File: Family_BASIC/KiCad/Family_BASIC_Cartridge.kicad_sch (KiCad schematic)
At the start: 0 parts

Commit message: Schematic started
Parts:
- added IC1: CHR ROM (27C64), Package_DIP:DIP-28_W15.24mm, symbol Memory_EPROM:27C64
- added IC2: PRG ROM (27256), Package_DIP:DIP-28_W15.24mm, symbol Memory_EPROM:27C256
- added IC4: 74HCT20, symbol 74xx:74LS20
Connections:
- new net A0: IC1.10 (A0), IC2.10 (A0)
- new net A1: IC1.9 (A1), IC2.9 (A1)
- new net A10: IC1.21 (A10), IC2.21 (A10)
- new net A11: IC1.23 (A11), IC2.23 (A11)
- new net A12: IC1.2 (A12), IC2.2 (A12)
- new net A13: IC2.26 (A13)
- new net A14: IC2.27 (A14)
- new net A2: IC1.8 (A2), IC2.8 (A2)
- new net A3: IC1.7 (A3), IC2.7 (A3)
- new net A4: IC1.6 (A4), IC2.6 (A4)
- new net A5: IC1.5 (A5), IC2.5 (A5)
- new net A6: IC1.4 (A6), IC2.4 (A6)
- new net A7: IC1.3 (A7), IC2.3 (A7)
- new net A8: IC1.25 (A8), IC2.25 (A8)
- new net A9: IC1.24 (A9), IC2.24 (A9)
- new net GND: IC1.14 (GND), IC2.14 (GND), IC2.20 (~{CE})
- new net PA13: IC1.22 (~{OE})
- new net V_{CC}: IC1.1 (VPP), IC1.27 (~{PGM}), IC1.28 (VCC), IC2.1 (VPP), IC2.28 (VCC)
- new net ~{RD}: IC1.20 (~{CE})
- new net ~{ROMSEL}: IC2.22 (~{OE})

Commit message: Schematic design progression
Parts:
- added BT1: 3V, symbol Device:Battery_Cell
- added C1: 68pF, symbol Device:C
- added C2, C3, C4, C5: 100nF, symbol Device:C
- added D1, D2: D, symbol Device:D
- added H1: Famicom_Cartridge_Edge, famicom:Famicom Cartridge Edge Connector (long legs), symbol Clueless_Engineer:Famicom_Cartridge_Edge
- added IC1: Working RAM (62256), Package_DIP:DIP-28_W15.24mm, symbol Memory_RAM:HM62256BLP
- added R1: 5.1KΩ, symbol Device:R
- renumbered IC4 to IC3, IC1 to IC4
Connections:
- net A13 is gone; now on net A_{13}: IC2.26 (A13)
- net A14 is gone; now on net A_{14}: IC2.27 (A14)
- net GND: now also IC3.10, IC3.12, IC3.13, IC3.7 (GND), IC3.9, BT1.2 (-), C1.2, C2.2, C3.2, C4.2, C5.2, H1.1 (GND), H1.16 (GND), IC1.14 (GND), IC1.22 (~{OE})
- net V_{CC}: now also IC3.14 (VCC), C2.1, C3.1, C4.1, C5.1, H1.30 (VCC), H1.31 (VCC)
- net ~{RD}: now also H1.17 (p~{RD})
- net ~{ROMSEL}: now also IC3.1, H1.44 (~{ROMSEL})
- net A_{13}: now reaches IC3.2
- net A_{13}: now also H1.34 (cA13)
- net A_{14}: now reaches IC3.4
- net A_{14}: now also H1.35 (cA14)
- net at IC3.6: now also C1.1, R1.2
- net PD_{0}: now reaches IC4.11 (D0)
- net PD_{0}: now also H1.26 (pD0)
- net PD_{1}: now reaches IC4.12 (D1)
- net PD_{1}: now also H1.27 (pD1)
- net PD_{2}: now reaches IC4.13 (D2)
- net PD_{2}: now also H1.28 (pD2)
- net PD_{3}: now reaches IC4.15 (D3)
- net PD_{3}: now also H1.29 (pD3)
- net PD_{4}: now reaches IC4.16 (D4)
- net PD_{4}: now also H1.60 (pD4)
- net PD_{5}: now reaches IC4.17 (D5)
- net PD_{5}: now also H1.59 (pD5)
- net PD_{6}: now reaches IC4.18 (D6)
- net PD_{6}: now also H1.58 (pD6)
- net PD_{7}: now reaches IC4.19 (D7)
- net PD_{7}: now also H1.57 (pD7)
- net D_{0}: now reaches IC2.11 (D0)
- net D_{0}: now also H1.43 (cD0), IC1.11 (Q0)
- net D_{1}: now reaches IC2.12 (D1)
- net D_{1}: now also H1.42 (cD1), IC1.12 (Q1)
- net D_{2}: now reaches IC2.13 (D2)
- net D_{2}: now also H1.41 (cD2), IC1.13 (Q2)
- net D_{3}: now reaches IC2.15 (D3)
- net D_{3}: now also H1.40 (cD3), IC1.15 (Q3)
- net D_{4}: now reaches IC2.16 (D4)
- net D_{4}: now also H1.39 (cD4), IC1.16 (Q4)
- net D_{5}: now reaches IC2.17 (D5)
- net D_{5}: now also H1.38 (cD5), IC1.17 (Q5)
- net D_{6}: now reaches IC2.18 (D6)
- net D_{6}: now also H1.37 (cD6), IC1.18 (Q6)
- net D_{7}: now reaches IC2.19 (D7)
- net D_{7}: now also H1.36 (cD7), IC1.19 (Q7)
- net A0 renamed A_{0}
- net A_{0}: now also H1.13 (cA0), IC1.10 (A0); no longer IC4.10 (A0)
- net A1 renamed A_{1}
- net A_{1}: now also H1.12 (cA1), IC1.9 (A1); no longer IC4.9 (A1)
- net A10 renamed A_{10}
- net A_{10}: now also H1.3 (cA10), IC1.21 (A10); no longer IC4.21 (A10)
- net A11 renamed A_{11}
- net A_{11}: now also H1.2 (cA11), IC1.23 (A11); no longer IC4.23 (A11)
- net A12 renamed A_{12}
- net A_{12}: now also H1.33 (cA12), IC1.2 (A12); no longer IC4.2 (A12)
- net A2 renamed A_{2}
- net A_{2}: now also H1.11 (cA2), IC1.8 (A2); no longer IC4.8 (A2)
- net A3 renamed A_{3}
- net A_{3}: now also H1.10 (cA3), IC1.7 (A3); no longer IC4.7 (A3)
- net A4 renamed A_{4}
- net A_{4}: now also H1.9 (cA4), IC1.6 (A4); no longer IC4.6 (A4)
- net A5 renamed A_{5}
- net A_{5}: now also H1.8 (cA5), IC1.5 (A5); no longer IC4.5 (A5)
- net A6 renamed A_{6}
- net A_{6}: now also H1.7 (cA6), IC1.4 (A6); no longer IC4.4 (A6)
- net A7 renamed A_{7}
- net A_{7}: now also H1.6 (cA7), IC1.3 (A7); no longer IC4.3 (A7)
- net A8 renamed A_{8}
- net A_{8}: now also H1.5 (cA8), IC1.25 (A8); no longer IC4.25 (A8)
- net A9 renamed A_{9}
- net A_{9}: now also H1.4 (cA9), IC1.24 (A9); no longer IC4.24 (A9)
- net PA13 renamed PA_{13}
- net PA_{13}: now also H1.56 (pA13)
- new net: D1.1 (K), D2.1 (K), R1.1
- new net: BT1.1 (+), D1.2 (A)
- new net: H1.45 (cAUDIO), H1.46 (rfAUDIO)
- new net: H1.48 (vram~{CE}), H1.49 (p~{A13})
- new net PA_{0}: H1.25 (pA0), IC4.10 (A0)
- new net PA_{10}: H1.18 (vramA10), H1.53 (pA10), IC4.21 (A10)
- new net PA_{11}: H1.54 (pA11), IC4.23 (A11)
- new net PA_{12}: H1.55 (pA12), IC4.2 (A12)
- new net PA_{1}: H1.24 (pA1), IC4.9 (A1)
- new net PA_{2}: H1.23 (pA2), IC4.8 (A2)
- new net PA_{3}: H1.22 (pA3), IC4.7 (A3)
- new net PA_{4}: H1.21 (pA4), IC4.6 (A4)
- new net PA_{5}: H1.20 (pA5), IC4.5 (A5)
- new net PA_{6}: H1.19 (pA6), IC4.4 (A6)
- new net PA_{7}: H1.50 (pA7), IC4.3 (A7)
- new net PA_{8}: H1.51 (pA8), IC4.25 (A8)
- new net PA_{9}: H1.52 (pA9), IC4.24 (A9)
- new net RAMV_{CC}: D2.2 (A), IC1.28 (VCC)
- new net RAM_{~{CS}}: IC1.20 (~{CS})
- new net R/_{W}: H1.14 (cR~{W})
- new net R/~{W}: IC1.27 (~{WE})
- no-connect marks 0 -> 4
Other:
- note added: "Unused Gate"
- note added: "WORK IN PROGRESS"
- company: (none) -> Brett Hallen
- title: (none) -> Nintendo Famicom Family BASIC 8KB
- moved on the sheet: IC2, IC3A, IC3B, IC4

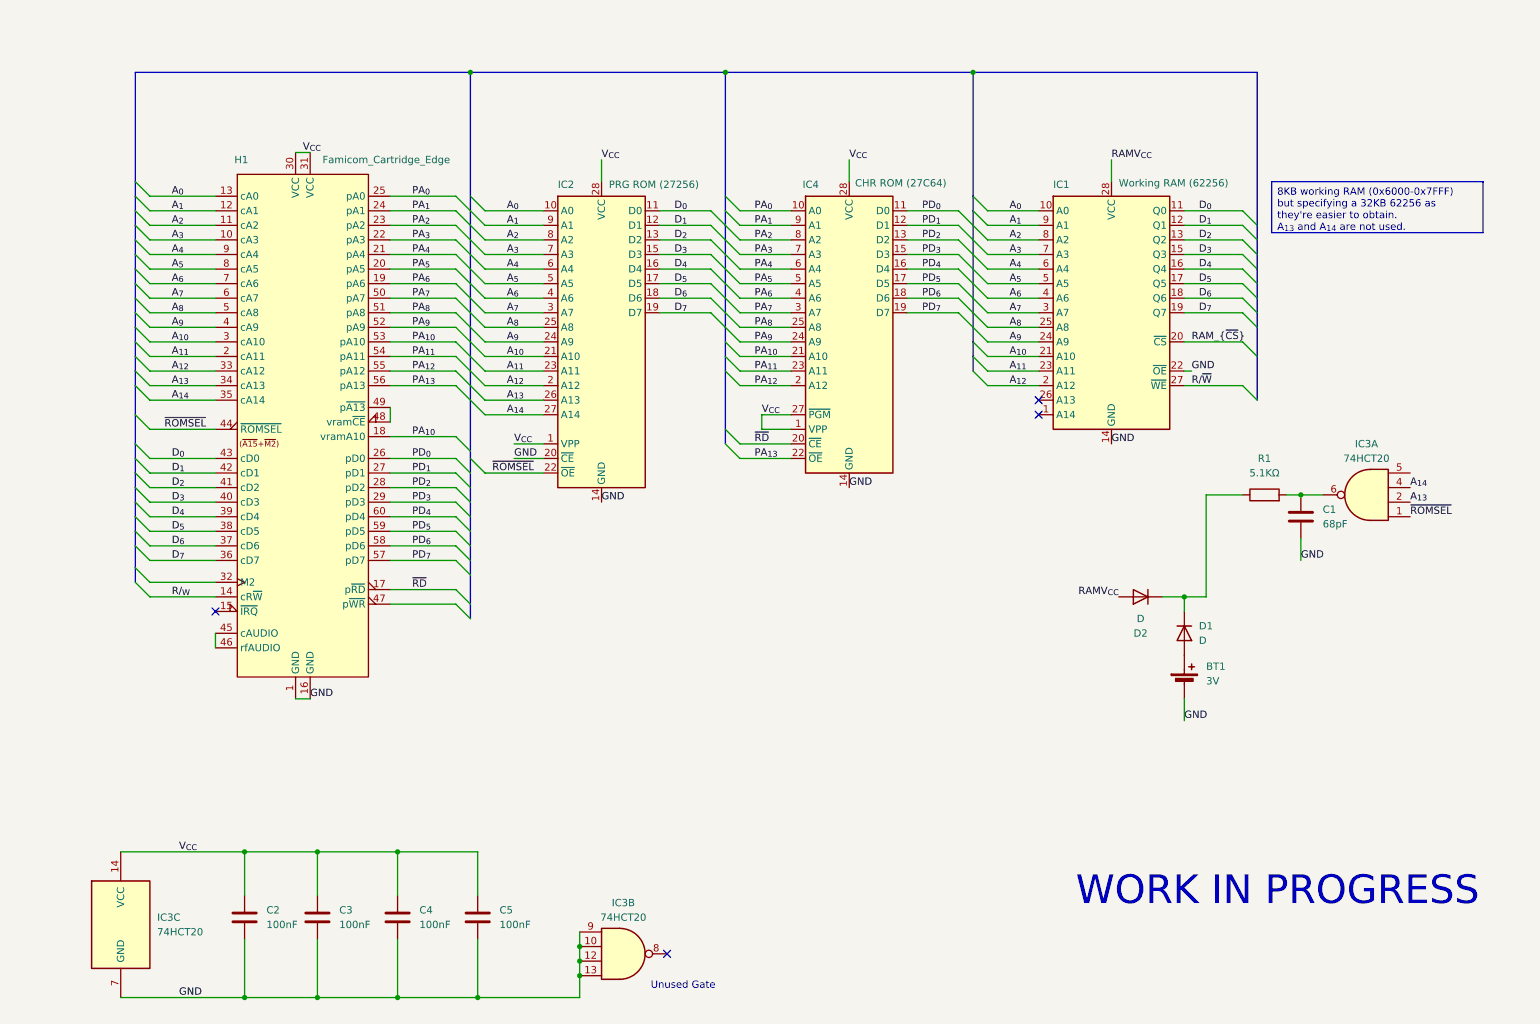
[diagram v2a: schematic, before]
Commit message: Initial schematic completed
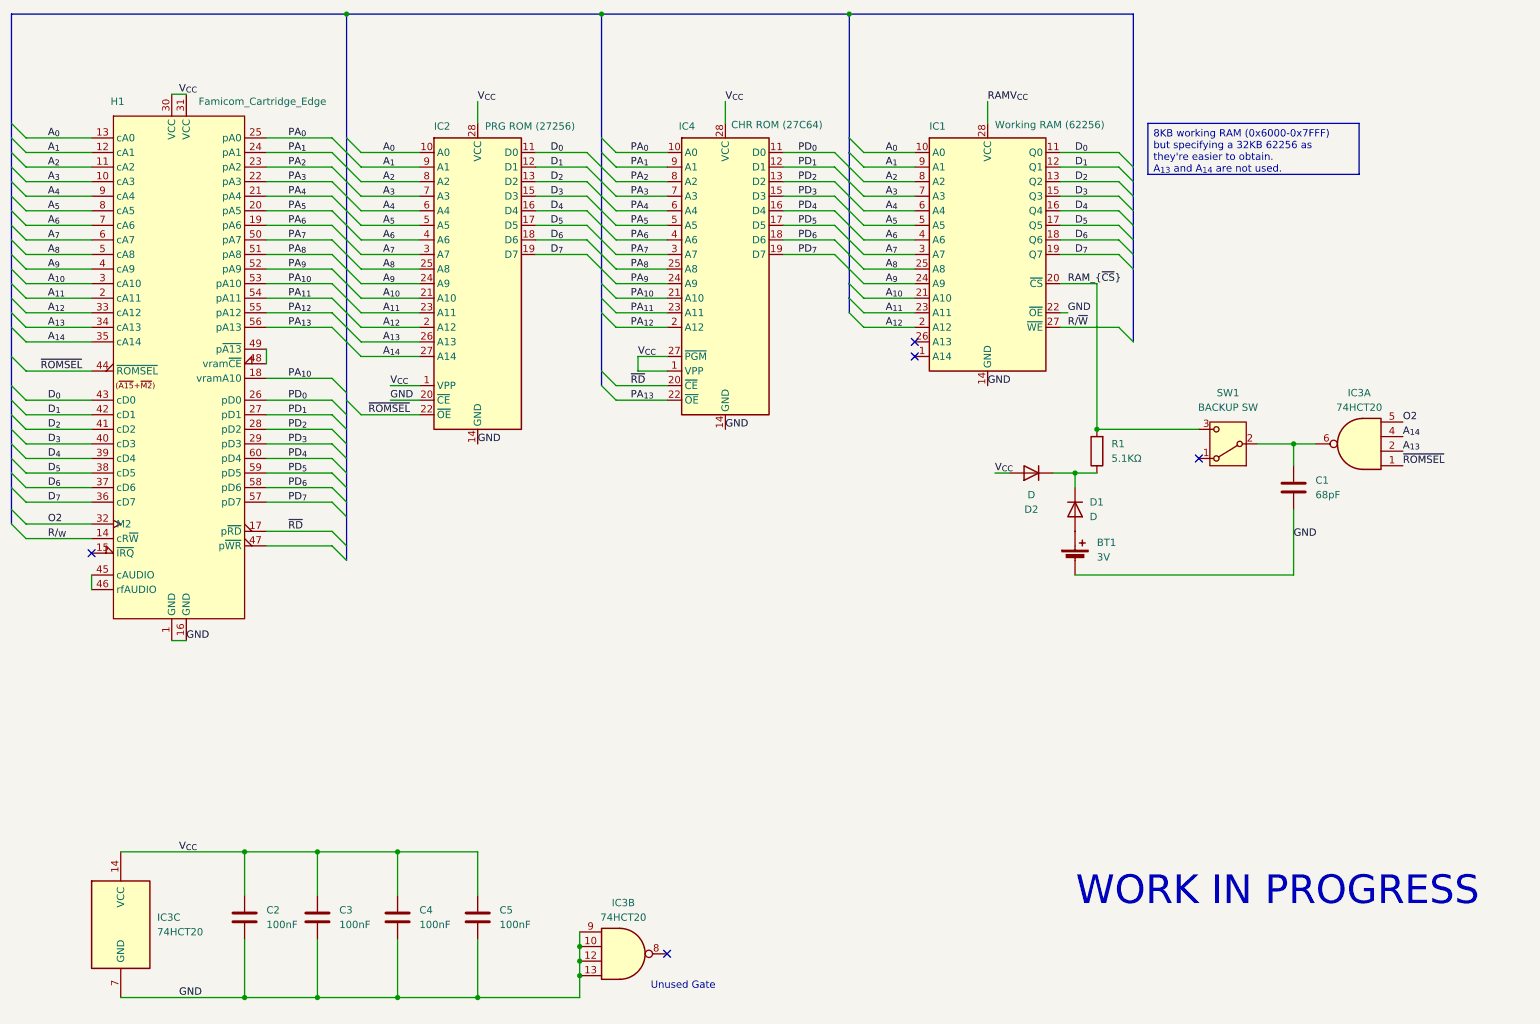
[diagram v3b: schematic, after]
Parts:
- added SW1: BACKUP SW, symbol Switch:SW_SPDT
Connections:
- net RAMV_{CC}: no longer D2.2 (A)
- net RAM_{~{CS}}: now also R1.2, SW1.3 (C)
- net V_{CC}: now also D2.2 (A)
- net O2: now reaches IC3.5
- net O2: now also H1.32 (M2)
- net at C1.1, IC3.6: now also SW1.2 (B); no longer R1.2
- no-connect marks 4 -> 5
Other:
- moved on the sheet: BT1, C1, D1, D2, H1, IC1, IC2, IC3A, IC4, R1

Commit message: Added DIP switch for RAM bank selection
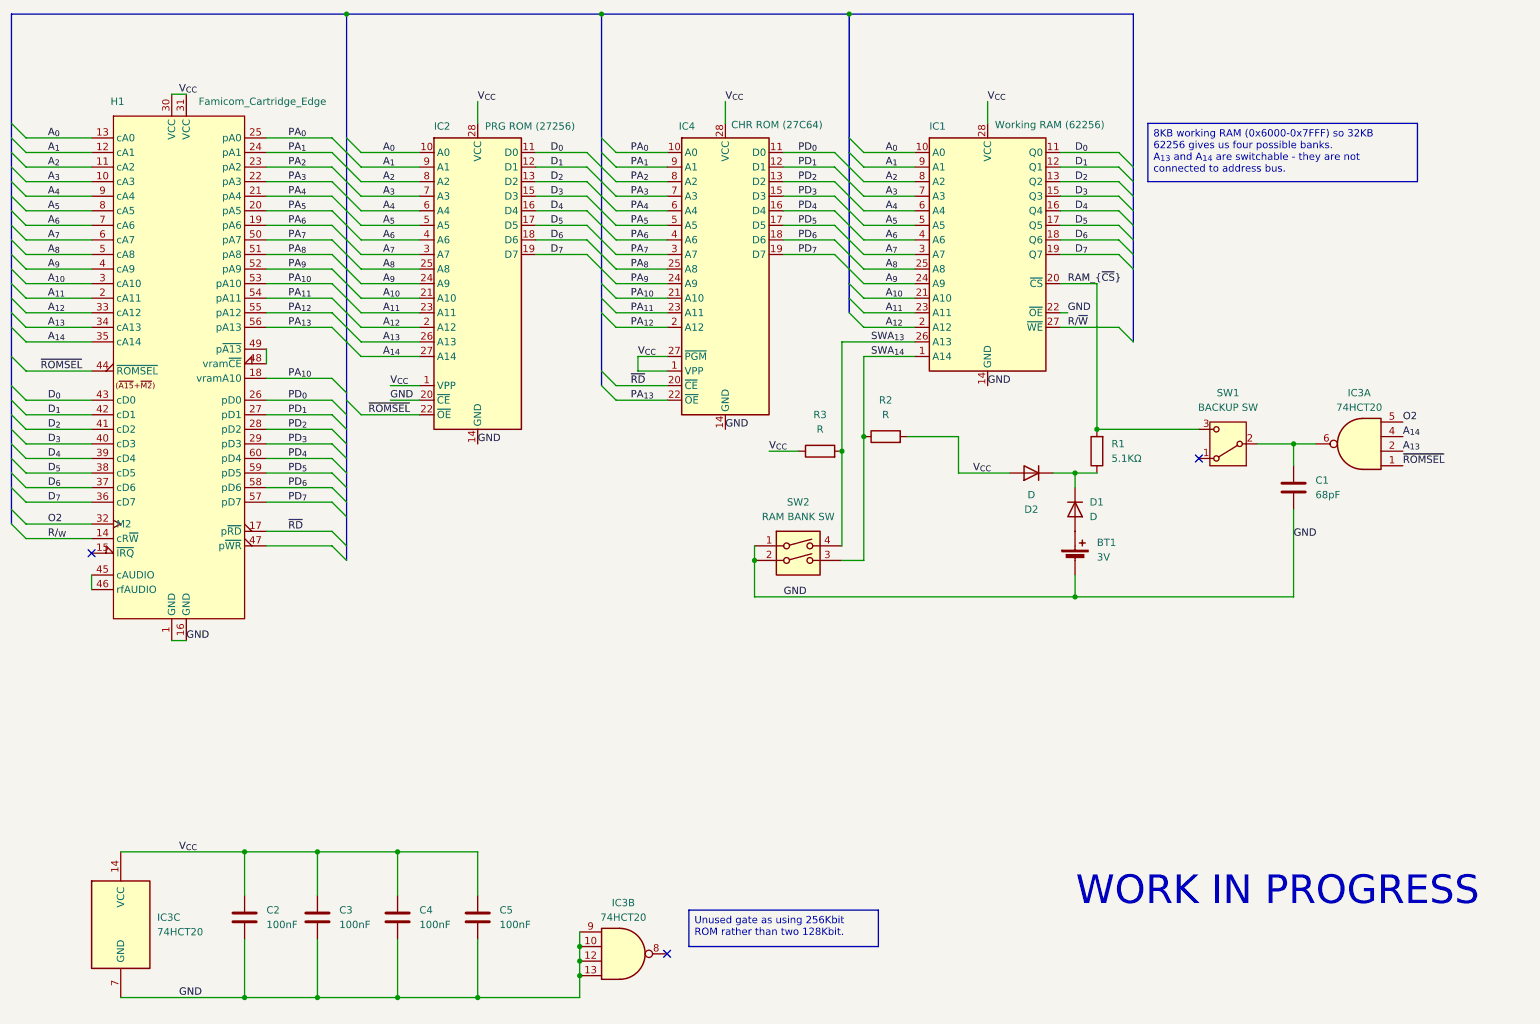
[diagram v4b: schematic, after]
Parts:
- added R2, R3: R, symbol Device:R
- added SW2: RAM BANK SW, symbol Switch:SW_DIP_x02
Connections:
- net RAMV_{CC} is gone; now on net V_{CC}: IC1.28 (VCC)
- net GND: now also SW2.1, SW2.2
- net V_{CC}: now also R2.2, R3.1
- net SWA_{14}: now reaches IC1.1 (A14)
- net SWA_{14}: now also R2.1, SW2.3
- net SWA_{13}: now reaches IC1.26 (A13)
- net SWA_{13}: now also R3.2, SW2.4
- no-connect marks 5 -> 3
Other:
- note removed: "Unused Gate"

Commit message: Update Family_BASIC_Cartridge.kicad_sch
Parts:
- C1, C2, C3, C4, C5: footprint (none) -> Capacitor_THT:C_Axial_L3.8mm_D2.6mm_P7.50mm_Horizontal
- H1: footprint famicom:Famicom Cartridge Edge Connector (long legs) -> Clueless_Engineer:Famicom_Cartridge_Edge_Connector_(long_legs)
- IC3: footprint (none) -> Package_DIP:DIP-14_W7.62mm
- R2, R3: value R -> 10KΩ
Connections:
- net SWA_{13}: now also R3.1; no longer R3.2
- net V_{CC}: now also R3.2; no longer IC1.28 (VCC), R3.1
- net RAMV_{CC}: now reaches D1.1 (K), D2.1 (K), R1.1
- net RAMV_{CC}: now also IC1.28 (VCC)
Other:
- moved on the sheet: C1, IC3A, IC3B, R1, R2, R3, SW1, SW2
